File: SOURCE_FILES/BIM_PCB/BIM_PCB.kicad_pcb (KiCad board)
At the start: 2 copper layers, 58.6 x 72.5 mm, 167 parts, among them J1 POWER INPUT, J2 Conn_02x03_Odd_Even, J3 Conn_01x06, J4 Conn_02x05_Odd_Even, J5 SIM_Card, J6 Conn_02x02_Odd_Even, Q1 SSM3J328R-HXY, Q10 2N7002, Q11 2N7002, Q2 BSS123, Q3 BSS123, Q4 BSN20, Q5 BSN20, Q6 2N7002, Q7 2N7002, Q8 2N7002, Q9 2N7002, SW1 reset, U1 STM32F103C8Tx, U2 PCF8523TK, U3 SIM7000G, U4 TBU-CA065-200-WH, U5 MAX485E, U6 TBU-CA065-200-WH, U7 ADP2504ACPZ-R7_3.3V_VERSION, U8 W25Q32JVSS, U9 ATA6561-GAQW-N, Y1 8MHz, Y2 32.678KHz, Y3 32.678KHz

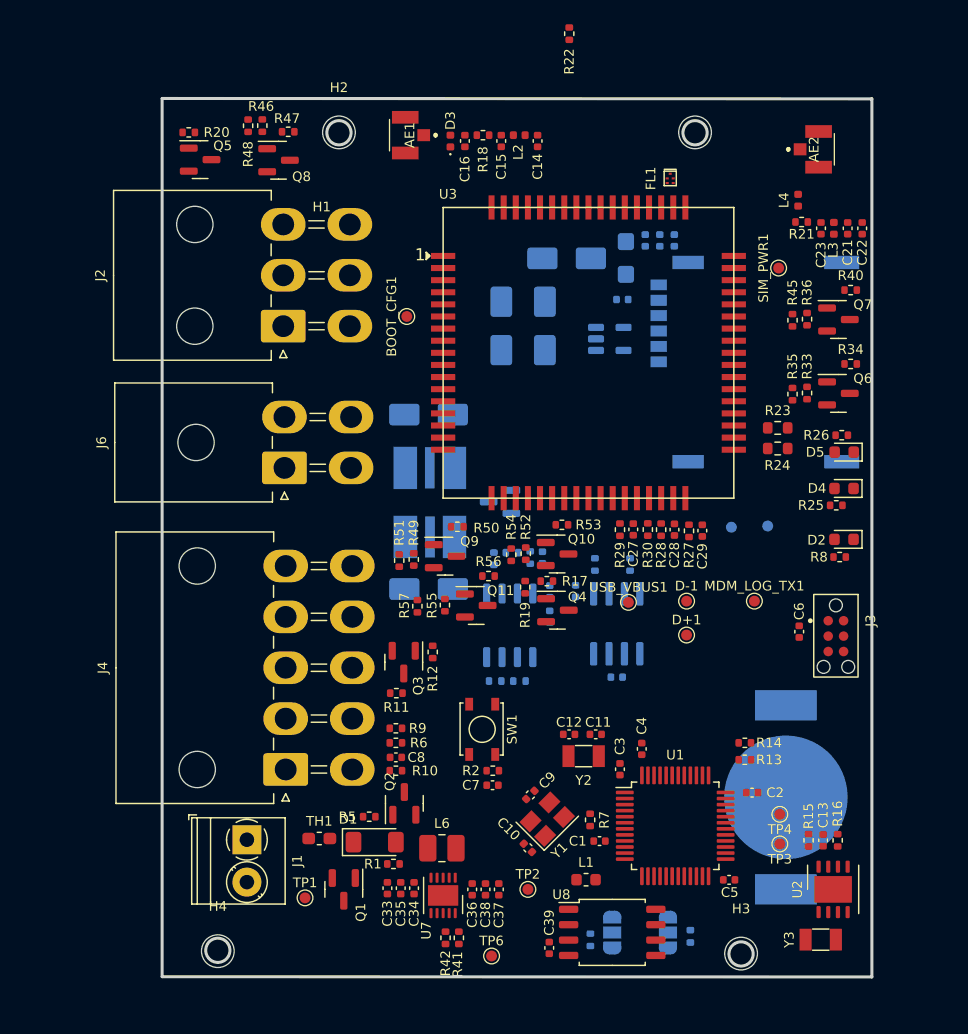
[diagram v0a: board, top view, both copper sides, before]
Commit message: completed design PCN and Images
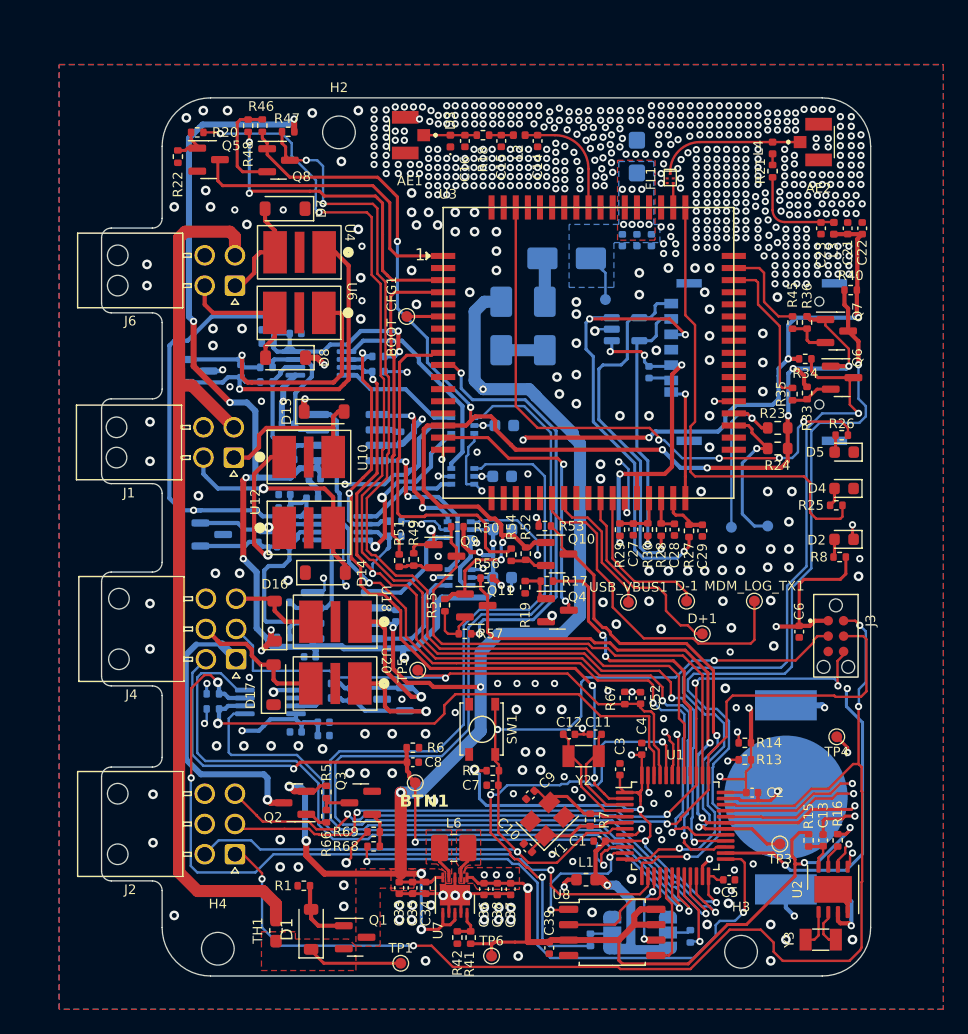
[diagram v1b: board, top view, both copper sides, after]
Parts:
- removed H1: MountingHole, MountingHole:MountingHole_2.7mm
- added C24: 100n, Capacitor_SMD:C_0402_1005Metric, B.Cu at (46.1, 90.5)
- added C25: 100n, Capacitor_SMD:C_0402_1005Metric, B.Cu at (46.1, 91.6)
- added C42: 10u, Capacitor_SMD:C_0402_1005Metric, B.Cu at (48.4, 90.8)
- added C43: 100n, Capacitor_SMD:C_0402_1005Metric, B.Cu at (55.3, 100.5)
- added C44: 100n, Capacitor_SMD:C_0402_1005Metric, B.Cu at (48.2, 103.9)
- added C45: 100n, Capacitor_SMD:C_0603_1608Metric, B.Cu at (64.1, 93.4)
- added C46: 100n, Capacitor_SMD:C_0603_1608Metric, B.Cu at (64.1, 97.4)
- added C47: 100n, Capacitor_SMD:C_0603_1608Metric, B.Cu at (64.2, 84.8)
- added C48: 100n, Capacitor_SMD:C_0603_1608Metric, B.Cu at (64.1, 89.0)
- added C49: 100n, Capacitor_SMD:C_0402_1005Metric, B.Cu at (49.3, 110.4)
- added C50: 100n, Capacitor_SMD:C_0402_1005Metric, B.Cu at (49.3, 109.3)
- added C51: 10u, Capacitor_SMD:C_0402_1005Metric, B.Cu at (47.0, 110.1)
- added C52: 100n, Capacitor_SMD:C_0402_1005Metric, F.Cu at (75.5, 107.3)
- added D13: BEP0080MA, Diode_SMD:D_SOD-123, F.Cu at (49.4, 83.7)
- added D14: BEP0080MA, Diode_SMD:D_SOD-123, F.Cu at (49.5, 97.0)
- added D15: ESDONCAN1LT1G, Package_TO_SOT_SMD:SOT-23, B.Cu at (40.1, 93.8)
- added D16: BEP0080MA, Diode_SMD:D_SOD-123, F.Cu at (45.3, 101.0)
- added D17: BEP0080MA, Diode_SMD:D_SOD-123, F.Cu at (45.2, 106.2)
- added D18: ESDONCAN1LT1G, Package_TO_SOT_SMD:SOT-23, B.Cu at (55.1, 107.4)
- added R58: 100K, Resistor_SMD:R_0402_1005Metric, B.Cu at (55.2, 94.0)
- added R59: 60R, Resistor_SMD:R_0402_1005Metric, B.Cu at (46.0, 102.3)
- added R60: 60R, Resistor_SMD:R_0402_1005Metric, B.Cu at (46.0, 99.4)
- added R61: 100K, Resistor_SMD:R_0402_1005Metric, B.Cu at (40.2, 108.2)
- added R62: 10R, Resistor_SMD:R_0402_1005Metric, B.Cu at (49.4, 106.1)
- added R63: 220R, Resistor_SMD:R_0402_1005Metric, B.Cu at (51.5, 107.0)
- added R64: 10R, Resistor_SMD:R_0402_1005Metric, B.Cu at (49.4, 107.3)
- added R65: 100K, Resistor_SMD:R_0402_1005Metric, B.Cu at (40.2, 107.0)
- added R66: 1k, Resistor_SMD:R_0402_1005Metric, F.Cu at (49.6, 117.1)
- added R67: 10K, Resistor_SMD:R_0402_1005Metric, F.Cu at (74.2, 107.3)
- added R68: 100R, Resistor_SMD:R_0402_1005Metric, F.Cu at (53.5, 119.5)
- added R69: 10K, Resistor_SMD:R_0402_1005Metric, F.Cu at (53.5, 118.3)
- added TP5: BTN2, brilliant-kicad-library:TestPoint_Pad_D0.9mm, F.Cu at (57.1, 105.0)
- added U10: TBU-CA065-200-WH, MACHADA_footprints:TBU-CA065-200-WH, F.Cu at (46.1, 87.4)
- added U11: SSP3485U, Package_SO:MSOP-8_3x3mm_P0.65mm, B.Cu at (50.5, 93.3)
- added U12: TBU-CA065-200-WH, MACHADA_footprints:TBU-CA065-200-WH, F.Cu at (46.1, 93.2)
- added U13: ATA6561-GAQW-N, Package_SO:SOIC-8_3.9x4.9mm_P1.27mm, B.Cu at (50.9, 100.5)
- added U14: WAS3157B, Package_TO_SOT_SMD:SOT-363_SC-70-6, B.Cu at (60.5, 93.4)
- added U15: WAS3157B, Package_TO_SOT_SMD:SOT-363_SC-70-6, B.Cu at (60.6, 97.3)
- added U16: WAS3157B, Package_TO_SOT_SMD:SOT-363_SC-70-6, B.Cu at (60.8, 84.8)
- added U17: WAS3157B, Package_TO_SOT_SMD:SOT-363_SC-70-6, B.Cu at (60.8, 89.0)
- added U18: TBU-CA065-200-WH, MACHADA_footprints:TBU-CA065-200-WH, F.Cu at (52.3, 101.0)
- added U19: SSP3485U, Package_SO:MSOP-8_3x3mm_P0.65mm, B.Cu at (44.9, 107.6)
- added U20: TBU-CA065-200-WH, MACHADA_footprints:TBU-CA065-200-WH, F.Cu at (52.3, 106.1)
- D1: footprint Diode_SMD:D_MiniMELF -> Diode_SMD:D_SOD-123
- D7, D8: value P0640TA -> BEP0080MA; footprint Diode_SMD:D_SMA -> Diode_SMD:D_SOD-123; moved to F.Cu
- J1: value POWER INPUT -> Conn_02x02_Odd_Even; footprint TerminalBlock_Phoenix:TerminalBlock_Phoenix_PT-1,5-2-3.5-H_1x02_P3.50mm_Horizontal -> Connector_Molex:Molex_Nano-Fit_105314-xx04_2x02_P2.50mm_Horizontal
- J2: footprint Connector_Molex:Molex_Mini-Fit_Jr_5569-06A2_2x03_P4.20mm_Horizontal -> Connector_Molex:Molex_Nano-Fit_105314-xx06_2x03_P2.50mm_Horizontal
- J4: value Conn_02x05_Odd_Even -> DISPLAY CONNECTOR; footprint Connector_Molex:Molex_Mini-Fit_Jr_5569-10A2_2x05_P4.20mm_Horizontal -> Connector_Molex:Molex_Nano-Fit_105314-xx06_2x03_P2.50mm_Horizontal
- J5: value SIM_Card -> nano_sim; footprint MACHADA_footprints:sim_micro_SMC2026 -> greencharge-footprints:GCT_SIM8066-6-1-14-01-A_REVA
- J6: footprint Connector_Molex:Molex_Mini-Fit_Jr_5569-04A2_2x02_P4.20mm_Horizontal -> Connector_Molex:Molex_Nano-Fit_105314-xx04_2x02_P2.50mm_Horizontal
- Q2: value BSS123 -> SSM3J328R-HXY
- Q3: value BSS123 -> IRLML0100TRPBF
- R10: value 10K -> 10R; moved to B.Cu
- R11, SIM_PWR1: moved to B.Cu
- R12: value 1K -> 10R; moved to B.Cu
- R5: value 1K -> 10K
- R9: value 10K -> 100K; moved to B.Cu
- U4, U6: moved to F.Cu
- U5: value MAX485E -> SSP3485U; footprint Package_SO:SOP-8_3.9x4.9mm_P1.27mm -> Package_SO:MSOP-8_3x3mm_P0.65mm
- moved J2 43.8 mm to (42.0, 120.2), turned to 180 degrees
- moved R22 33.9 mm to (37.3, 62.6)
- moved C31 32.4 mm to (44.7, 78.0), turned to 180 degrees
- moved C30 31.8 mm to (44.7, 76.9), turned to 180 degrees
- moved J1 31.6 mm to (41.9, 87.5), turned to 180 degrees
- moved R44 30.5 mm to (46.4, 84.7), turned to 180 degrees
- moved R31 29.2 mm to (53.9, 79.1)
- moved C32 27.5 mm to (47.0, 77.2), turned to 0 degrees
- moved R32 27.3 mm to (53.9, 80.3), turned to 180 degrees
- moved D9 27.2 mm to (38.9, 80.3), turned to 0 degrees
- moved U9 27.0 mm to (51.3, 85.8), turned to 180 degrees
- moved R38 26.9 mm to (42.5, 80.3), turned to -90 degrees
- moved R43 26.8 mm to (46.4, 87.6), turned to 180 degrees
- moved U5 26.7 mm to (49.1, 79.7), turned to 180 degrees
- moved C40 26.6 mm to (55.7, 85.8), turned to 90 degrees
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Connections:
- net /CAN_TRANSCEIVER_ATA6561/CAN_STBY renamed /CAN_STBY
- net /RS485_MAX485/RS485_DE renamed /RS485_DE
- C8 pad 1: /STM32FC8T6_MCU/BUTTON -> /BUTTON
- D7 pad 2: /RS485_MAX485/B -> /RS485_MAX485/A
- D8 pad 2: /RS485_MAX485/A -> /RS485_MAX485/B
- J1 pad 1: /VIN -> /RS485_MAX486/A
- J1 pad 2: GND -> VIN
- J4 pad 1: /STM32FC8T6_MCU/DI -> Net-(J4-Pin_1)
- J4 pad 2: +3V3 -> /Button_2
- J4 pad 3: /STM32FC8T6_MCU/SCK -> /RS485_MAX487/A
- J4 pad 4: /STM32FC8T6_MCU/Backlight -> /BUTTON
- J4 pad 5: /STM32FC8T6_MCU/DC -> /RS485_MAX487/B
- J4 pad 6: /STM32FC8T6_MCU/Buzzer -> GND
- J6 pad 2: +5V -> VIN
- Q2 pad 2: GND -> unconnected-(Q2-S-Pad2)
- Q2 pad 3: /STM32FC8T6_MCU/Buzzer -> Net-(J4-Pin_1)
- R10 pad 1: /STM32FC8T6_MCU/LCD_CS -> /CAN_TRANSCEIVER_ATA6562/A_to_CANL
- R10 pad 2: +3V3 -> Net-(U10-line_in)
- R11 pad 1: Net-(Q3-D) -> Net-(U12-line_in)
- R11 pad 2: /STM32FC8T6_MCU/Backlight -> Net-(U10-line_in)
- R12 pad 1: /STM32FC8T6_MCU/LCD_LED -> /CAN_TRANSCEIVER_ATA6562/B_to_CANH
- R12 pad 2: Net-(Q3-G) -> Net-(U12-line_in)
- R31 pad 1: /RS485_MAX485/RS485_~{RE} -> /RS485_~{RE}
- R35 pad 1: /SIM7000_GPRS_MODULE/MOSFET_LOGIC_LEVEL_TRANSLATOR2/LOW_SIDE_LOGIC_SIGNAL -> unconnected-(R35-Pad1)
- R37 pad 1: B_to_CANH -> /CAN_TRANSCEIVER_ATA6561/A_to_CANL
- R39 pad 1: A_to_CANL -> /CAN_TRANSCEIVER_ATA6561/B_to_CANH
- R43 pad 1: A_to_CANL -> /CAN_TRANSCEIVER_ATA6561/A_to_CANL
- R44 pad 1: B_to_CANH -> /CAN_TRANSCEIVER_ATA6561/B_to_CANH
- R45 pad 1: /SIM7000_GPRS_MODULE/MOSFET_LOGIC_LEVEL_TRANSLATOR3/LOW_SIDE_LOGIC_SIGNAL -> unconnected-(R45-Pad1)
- R48 pad 1: /SIM7000_GPRS_MODULE/MOSFET_LOGIC_LEVEL_TRANSLATOR/LOW_SIDE_LOGIC_SIGNAL -> unconnected-(R48-Pad1)
- R5 pad 1: /STM32FC8T6_MCU/BUZZER -> +5V
- R5 pad 2: Net-(Q2-G) -> Net-(Q3-D)
- R51 pad 1: /SIM7000_GPRS_MODULE/MOSFET_LOGIC_LEVEL_TRANSLATOR5/LOW_SIDE_LOGIC_SIGNAL -> unconnected-(R51-Pad1)
- R54 pad 1: /SIM7000_GPRS_MODULE/MOSFET_LOGIC_LEVEL_TRANSLATOR1/LOW_SIDE_LOGIC_SIGNAL -> unconnected-(R54-Pad1)
- R57 pad 1: /SIM7000_GPRS_MODULE/MOSFET_LOGIC_LEVEL_TRANSLATOR4/LOW_SIDE_LOGIC_SIGNAL -> unconnected-(R57-Pad1)
- R6 pad 1: /STM32FC8T6_MCU/BUTTON -> /BUTTON
- R9 pad 1: /STM32FC8T6_MCU/RST -> /RS485_~{RE}
- R9 pad 2: +3V3 -> +3.3VA
- TH1 pad 1: /VIN -> VIN
- TP2 pad 1: /STM32FC8T6_MCU/BUTTON -> /BUTTON
- U1 pad 10: /STM32FC8T6_MCU/BUTTON -> /BUTTON
- U1 pad 14: /STM32FC8T6_MCU/LCD_CS -> /RS485_MAX487/RS485_DE
- U1 pad 15: /STM32FC8T6_MCU/SCK -> /FLASH_MEMORY/SCK
- U1 pad 17: /STM32FC8T6_MCU/DI -> /FLASH_MEMORY/MOSI
- U1 pad 18: /STM32FC8T6_MCU/DC -> /SOFT_DISPLAY_RS485_DI
- U1 pad 19: /STM32FC8T6_MCU/RST -> /SOFT_DISPLAY_RS485_RO
- U1 pad 2: /RS485_MAX485/RS485_~{RE} -> /RS485_~{RE}
- U1 pad 21: /RS485_MAX485/RS485_RO -> /MULTIPLEXER_SWITCH_WAS3157B-7/SIG2_IN
- U1 pad 22: /RS485_MAX485/RS485_DI -> /MULTIPLEXER_SWITCH_WAS3157B-7/SIG1_IN
- U1 pad 25: /RTC_MODULE_IC_PCF8523/RTC_~{INT} -> /DISPLAY_PWR_EN
- U1 pad 32: /CAN_TRANSCEIVER_ATA6561/CAN_RX -> /MULTIPLEXER_SWITCH_WAS3157B-6/SIG2_IN
- U1 pad 33: /CAN_TRANSCEIVER_ATA6561/CAN_TX -> /MULTIPLEXER_SWITCH_WAS3157B-6/SIG1_IN
- U1 pad 45: /STM32FC8T6_MCU/Buzzer -> /Button_2
- U1 pad 46: /STM32FC8T6_MCU/LCD_LED -> /RS485_MAX487/RS485_~{RE}
- U4 pad 2: /RS485_MAX485/B -> /RS485_MAX485/A
- U5 pad 1: /RS485_MAX485/RS485_RO -> /MULTIPLEXER_SWITCH_WAS3157B-7/OUT2_NC
- U5 pad 2: /RS485_MAX485/RS485_~{RE} -> /RS485_~{RE}
- U5 pad 4: /RS485_MAX485/RS485_DI -> /MULTIPLEXER_SWITCH_WAS3157B-7/OUT1_NC
- U5 pad 6: A_to_CANL -> /CAN_TRANSCEIVER_ATA6561/A_to_CANL
- U5 pad 7: B_to_CANH -> /CAN_TRANSCEIVER_ATA6561/B_to_CANH
- U6 pad 2: /RS485_MAX485/A -> /RS485_MAX485/B
- U8 pad 5: /STM32FC8T6_MCU/DI -> /FLASH_MEMORY/MOSI
- U8 pad 6: /STM32FC8T6_MCU/SCK -> /FLASH_MEMORY/SCK
- U9 pad 6: A_to_CANL -> /CAN_TRANSCEIVER_ATA6561/A_to_CANL
- U9 pad 7: B_to_CANH -> /CAN_TRANSCEIVER_ATA6561/B_to_CANH
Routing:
- net +3V3: track 0.00 -> 268.9 mm, vias 0 -> 23
- net VDD_EXT: track 0.00 -> 129.6 mm, vias 0 -> 10
- net +5V: track 0.00 -> 124.8 mm, vias 0 -> 9
- net +3.3VA: track 0.00 -> 113.4 mm, vias 0 -> 7
- net /STM32FC8T6_MCU/3v3_stm: track 0.00 -> 103.5 mm, vias 0 -> 9
- net /STM32FC8T6_MCU/swdio: track 0.00 -> 102.8 mm, vias 0 -> 4
- net /SIM7000_GPRS_MODULE/PWRKEY: track 0.00 -> 97.1 mm, vias 0 -> 4
- net /MULTIPLEXER_SWITCH_WAS3157B-7/SIG1_IN: track 0.00 -> 92.6 mm, vias 0 -> 1
- net GND: track 0.00 -> 89.8 mm, vias 0 -> 690
- net /MULTIPLEXER_SWITCH_WAS3157B-7/SIG2_IN: track 0.00 -> 87.3 mm, vias 0 -> 1
- net /SIM7000_GPRS_MODULE/Sim_DTR: track 0.00 -> 83.3 mm, vias 0 -> 2
- net /STM32FC8T6_MCU/RESET: track 0.00 -> 82.5 mm, vias 0 -> 3
- net VIN: track 0.00 -> 76.7 mm
- net /RS485_DE: track 0.00 -> 74.6 mm, vias 0 -> 4
- net /CAN_STBY: track 0.00 -> 70.1 mm, vias 0 -> 4
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- added copper zone on F.Cu, net +3V3
- added copper zone on F.Cu, net +5V
- added copper zone on B.Cu, net 4.2V_SIMPWR
- added copper zone on F.Cu, net 4.2V_SIMPWR
- added copper zone on B.Cu, net GND
- added copper zone on F.Cu, net GND
- added copper zone on In1.Cu, net GND
- added copper zone on In2.Cu, net GND
- added copper zone on F.Cu, net Net-(D1-K)
- added copper zone on F.Cu, net Net-(U7-SW1)
- added copper zone on F.Cu, net Net-(U7-SW2)
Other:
- board size 58.6 x 72.5 mm -> 63.5 x 72.5 mm
- copper layers 2 -> 4
- board text added: "BTN1"

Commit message: complete BIM Board
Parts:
- removed C47, C48: 100n, Capacitor_SMD:C_0603_1608Metric
- removed U16, U17: WAS3157B, Package_TO_SOT_SMD:SOT-363_SC-70-6
- added G***: LOGO, MACHADA_footprints:ECOBODDA, B.Cu at (63.5, 117.2)
- added G***: LOGO, MACHADA_footprints:GEVITON_LOGO_small, B.Cu at (83.4, 59.9)
- added TP7: PA4, brilliant-kicad-library:TestPoint_Pad_D0.9mm, B.Cu at (69.5, 125.3)
- added TP8: PB9, brilliant-kicad-library:TestPoint_Pad_D0.9mm, F.Cu at (66.8, 110.2)
- C20: value 100u -> 1000u; footprint Capacitor_Tantalum_SMD:CP_EIA-3216-18_Kemet-A -> Capacitor_Tantalum_SMD:CP_EIA-7343-43_Kemet-X
- J5: footprint greencharge-footprints:GCT_SIM8066-6-1-14-01-A_REVA -> MACHADA_footprints:nano_sim_NSIM-2-C
- R41: value 1K -> 0R
- U14, U15: value WAS3157B -> MC74HC4052A; footprint Package_TO_SOT_SMD:SOT-363_SC-70-6 -> Package_SO:SSOP-16_5.3x6.2mm_P0.65mm
- moved U14 7.74 mm to (62.2, 85.8), turned to -90 degrees
- moved C45 7.58 mm to (58.0, 88.9), turned to 90 degrees
- moved J5 6.69 mm to (79.2, 77.0)
- moved D6 6.62 mm to (76.7, 83.0), turned to -90 degrees
- moved C26 4.47 mm to (77.6, 76.2), turned to 90 degrees
- moved U15 3.79 mm to (63.3, 94.7)
- moved C46 2.76 mm to (66.4, 98.9), turned to 180 degrees
- moved R2 1.13 mm to (62.2, 113.3)
- moved C7 1.00 mm to (62.3, 114.5)
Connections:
- net Net-(D2-K) renamed /STM32FC8T6_MCU/SEL
- Q2 pad 2: unconnected-(Q2-S-Pad2) -> +5V
- R35 pad 1: unconnected-(R35-Pad1) -> /SIM7000_GPRS_MODULE/MOSFET_LOGIC_LEVEL_TRANSLATOR2/LOW_SIDE_LOGIC_SIGNAL
- R45 pad 1: unconnected-(R45-Pad1) -> /SIM7000_GPRS_MODULE/MOSFET_LOGIC_LEVEL_TRANSLATOR3/LOW_SIDE_LOGIC_SIGNAL
- R48 pad 1: unconnected-(R48-Pad1) -> /SIM7000_GPRS_MODULE/MOSFET_LOGIC_LEVEL_TRANSLATOR/LOW_SIDE_LOGIC_SIGNAL
- R51 pad 1: unconnected-(R51-Pad1) -> /SIM7000_GPRS_MODULE/MOSFET_LOGIC_LEVEL_TRANSLATOR5/LOW_SIDE_LOGIC_SIGNAL
- R54 pad 1: unconnected-(R54-Pad1) -> /SIM7000_GPRS_MODULE/MOSFET_LOGIC_LEVEL_TRANSLATOR1/LOW_SIDE_LOGIC_SIGNAL
- R57 pad 1: unconnected-(R57-Pad1) -> /SIM7000_GPRS_MODULE/MOSFET_LOGIC_LEVEL_TRANSLATOR4/LOW_SIDE_LOGIC_SIGNAL
- R61 pad 1: /RS485_MAX487/RS485_~{RE} -> /RS485_~{RE}
- R65 pad 2: /RS485_MAX487/RS485_DE -> /RS485_DE
- U1 pad 14: /RS485_MAX487/RS485_DE -> Net-(U1-PA4)
- U1 pad 18: /SOFT_DISPLAY_RS485_DI -> /MUX_SEL_A
- U1 pad 19: /SOFT_DISPLAY_RS485_RO -> /MUX_SEL_B
- U1 pad 21: /MULTIPLEXER_SWITCH_WAS3157B-7/SIG2_IN -> /STM32FC8T6_MCU/RS485_RO
- U1 pad 22: /MULTIPLEXER_SWITCH_WAS3157B-7/SIG1_IN -> /STM32FC8T6_MCU/RS485_DI
- U1 pad 32: /MULTIPLEXER_SWITCH_WAS3157B-6/SIG2_IN -> /STM32FC8T6_MCU/CAN_RX
- U1 pad 33: /MULTIPLEXER_SWITCH_WAS3157B-6/SIG1_IN -> /STM32FC8T6_MCU/CAN_TX
- U1 pad 46: /RS485_MAX487/RS485_~{RE} -> Net-(U1-PB9)
- U14 pad 1: /ecu_CAN_TX_2 -> /CAN_TX_2
- U14 pad 2: GND -> unconnected-(U14-Y2-Pad2)
- U14 pad 3: /CAN_TRANSCEIVER_ATA6561/CAN_TX -> /STM32FC8T6_MCU/CAN_TX
- U14 pad 4: /MULTIPLEXER_SWITCH_WAS3157B-6/SIG1_IN -> unconnected-(U14-Y3-Pad4)
- U14 pad 5: +3V3 -> /ecu_CAN_TX_2
- U14 pad 6: /SEL -> GND
- U15 pad 1: /ecu_CAN_RX_2 -> /RS485_D1
- U15 pad 2: GND -> /DISPLAY_RS485_DI
- U15 pad 3: /CAN_TRANSCEIVER_ATA6561/CAN_RX -> /STM32FC8T6_MCU/RS485_DI
- U15 pad 4: /MULTIPLEXER_SWITCH_WAS3157B-6/SIG2_IN -> unconnected-(U15-Y3-Pad4)
- U15 pad 5: +3V3 -> /ecu_RS485_DI
- U15 pad 6: /SEL -> GND
- U19 pad 1: /SOFT_DISPLAY_RS485_RO -> /DISPLAY_RS485_RO
- U19 pad 2: /RS485_MAX487/RS485_~{RE} -> /RS485_~{RE}
- U19 pad 3: /RS485_MAX487/RS485_DE -> /RS485_DE
- U19 pad 4: /SOFT_DISPLAY_RS485_DI -> /DISPLAY_RS485_DI
- U5 pad 1: /MULTIPLEXER_SWITCH_WAS3157B-7/OUT2_NC -> /RS485_RO
- U5 pad 4: /MULTIPLEXER_SWITCH_WAS3157B-7/OUT1_NC -> /RS485_D1
- U7 pad 11: (no net) -> GND
- U9 pad 1: /CAN_TRANSCEIVER_ATA6561/CAN_TX -> /CAN_TX_2
- U9 pad 4: /CAN_TRANSCEIVER_ATA6561/CAN_RX -> /CAN_RX_2
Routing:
- net /MULTIPLEXER_SWITCH_WAS3157B-7/SIG1_IN: track 92.6 -> 0.00 mm, vias 1 -> 0
- net /MULTIPLEXER_SWITCH_WAS3157B-7/SIG2_IN: track 87.3 -> 0.00 mm, vias 1 -> 0
- net /STM32FC8T6_MCU/RS485_DI: track 0.00 -> 76.8 mm, vias 0 -> 3
- net /STM32FC8T6_MCU/CAN_TX: track 0.00 -> 68.4 mm, vias 0 -> 2
- net /MUX_SEL_A: track 0.00 -> 67.4 mm, vias 0 -> 5
- net /STM32FC8T6_MCU/CAN_RX: track 0.00 -> 64.0 mm, vias 0 -> 2
- net /MUX_SEL_B: track 0.00 -> 63.3 mm, vias 0 -> 5
- net /RS485_MAX487/RS485_DE: track 62.7 -> 0.00 mm, vias 3 -> 0
- net /SOFT_DISPLAY_RS485_DI: track 61.2 -> 0.00 mm, vias 1 -> 0
- net /MULTIPLEXER_SWITCH_WAS3157B-6/SIG1_IN: track 59.7 -> 0.00 mm, vias 2 -> 0
- net /STM32FC8T6_MCU/RS485_RO: track 0.00 -> 57.6 mm, vias 0 -> 5
- net /MULTIPLEXER_SWITCH_WAS3157B-6/SIG2_IN: track 57.4 -> 0.00 mm, vias 2 -> 0
- net /SOFT_DISPLAY_RS485_RO: track 53.4 -> 0.00 mm, vias 1 -> 0
- net /RS485_MAX487/RS485_~{RE}: track 46.3 -> 0.00 mm, vias 1 -> 0
- net /RS485_~{RE}: track 64.8 -> 101.4 mm, vias 4 -> 6
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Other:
- board text added: "001221223"
- board text added: "3V3"
- board text added: "BTN2"
- board text added: "MADE IN KENYA"
- board text added: "PA4"
- board text added: "PB9"
- board text added: "PWR IN"
- board text added: "RX1"
- board text added: "TX1"
